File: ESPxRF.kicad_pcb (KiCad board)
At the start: 4 copper layers, 67.6 x 28.7 mm, 37 parts, among them J1 USB_C_Receptacle_USB2.0, J2 ANT, U1 NCP115ASN330T2G, U2 NRF24L01, U3 USBLC6-2SC6, U4 ESP32-S3, Y1 Crystal_GND24_Small

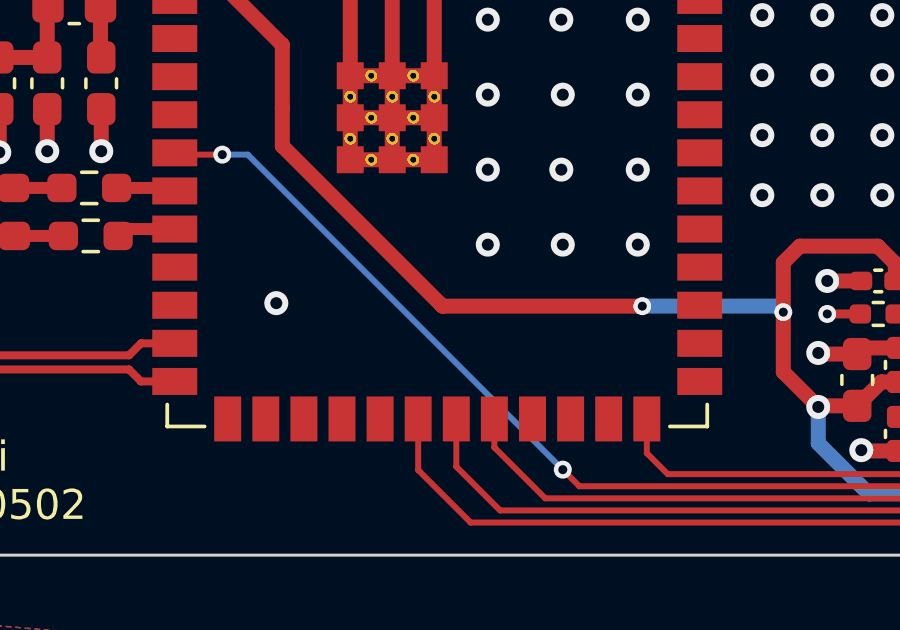
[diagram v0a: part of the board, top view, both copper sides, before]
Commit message: added jlc silkscreen tidied schematic
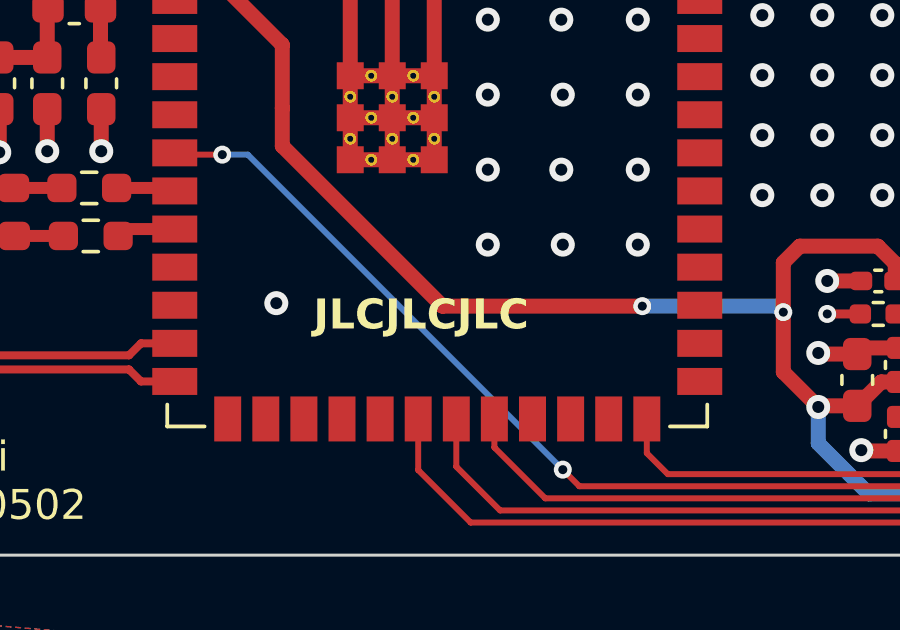
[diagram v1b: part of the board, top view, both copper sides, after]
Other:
- board text added: "JLCJLCJLC"
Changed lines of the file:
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@@
     (pad_to_mask_clearance 0)
     (pcbplotparams
-      (layerselection 0x00010fc_ffffffff)
+      (layerselection 0x00011fc_ffffffff)
       (plot_on_all_layers_selection 0x0000000_00000000)
       (disableapertmacros false)
@@
       (outputformat 1)
       (mirror false)
-      (drillshape 1)
+      (drillshape 0)
       (scaleselection 1)
-      (outputdirectory "")
+      (outputdirectory "Gerber/")
     )
   )
@@
     (fp_line (start 2 2) (end -2 2)
       (stroke (width 0.1) (type solid)) (layer "F.Fab"))
-    (pad "" smd roundrect (at -0.625 -0.625 90) (size 1.01 1.01) (layers "F.Paste") (roundrect_rratio 0.247525))
-    (pad "" smd roundrect (at -0.625 0.625 90) (size 1.01 1.01) (layers "F.Paste") (roundrect_rratio 0.247525))
-    (pad "" smd roundrect (at 0.625 -0.625 90) (size 1.01 1.01) (layers "F.Paste") (roundrect_rratio 0.247525))
-    (pad "" smd roundrect (at 0.625 0.625 90) (size 1.01 1.01) (layers "F.Paste") (roundrect_rratio 0.247525))
+    (pad "" smd roundrect (at -0.625 -0.625 90) (size 1.01 1.01) (layers "F.Paste") (roundrect_rratio 0.2475247525))
+    (pad "" smd roundrect (at -0.625 0.625 90) (size 1.01 1.01) (layers "F.Paste") (roundrect_rratio 0.2475247525))
+    (pad "" smd roundrect (at 0.625 -0.625 90) (size 1.01 1.01) (layers "F.Paste") (roundrect_rratio 0.2475247525))
+    (pad "" smd roundrect (at 0.625 0.625 90) (size 1.01 1.01) (layers "F.Paste") (roundrect_rratio 0.2475247525))
     (pad "1" smd roundrect (at -1.9375 -1 90) (size 0.825 0.25) (layers "F.Cu" "F.Paste" "F.Mask") (roundrect_rratio 0.25)
       (net 9 "CE") (pinfunction "CE") (pintype "input"))
@@
     (effects (font (size 1 1) (thickness 0.25) bold) (justify left bottom))
   )
+  (gr_text "JLCJLCJLC" (at 116.84 75.565) (layer "F.SilkS")
+    (effects (font (size 1 1) (thickness 0.25) bold) (justify left bottom))
+  )

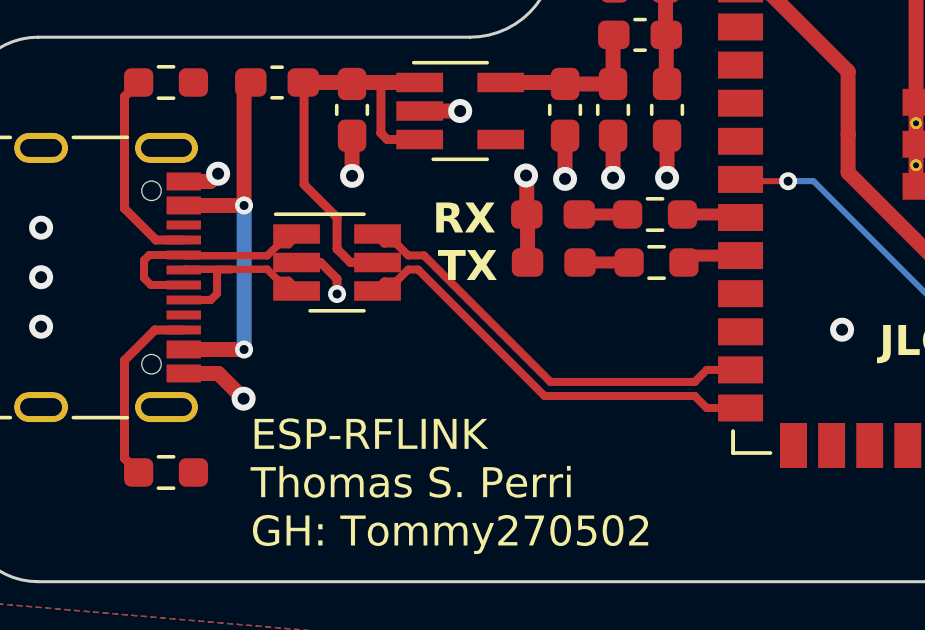
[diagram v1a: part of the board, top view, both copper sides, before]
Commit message: fixed short usb esd protection IC
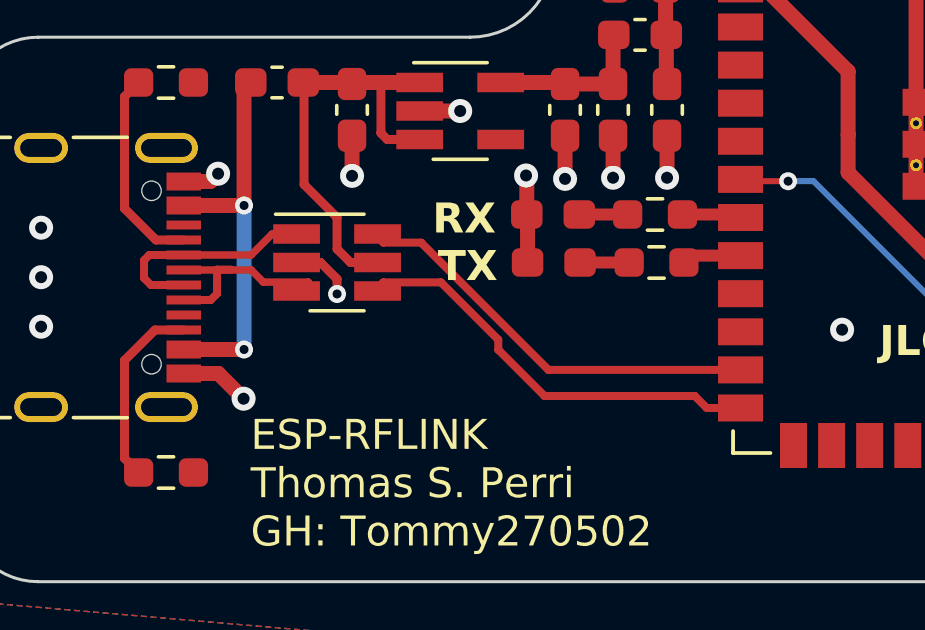
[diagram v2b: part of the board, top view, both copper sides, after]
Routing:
- net USBCON_D+: track 6.65 -> 7.22 mm
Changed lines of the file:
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@@
   (segment (start 137.0975 77.56) (end 136.265 78.3925) (width 0.2) (layer "F.Cu") (net 4))
   (segment (start 137.59 77.56) (end 137.0975 77.56) (width 0.2) (layer "F.Cu") (net 4))
-  (segment (start 93.655 72.61) (end 93.679999 72.585001) (width 0.25) (layer "F.Cu") (net 5))
   (segment (start 94.765163 73.398445) (end 94.765163 72.596803) (width 0.267208) (layer "F.Cu") (net 5))
   (segment (start 94.553608 73.61) (end 94.765163 73.398445) (width 0.267208) (layer "F.Cu") (net 5))
+  (segment (start 96.3068 73.0132) (end 97.8068 73.0132) (width 0.25) (layer "F.Cu") (net 5))
+  (segment (start 95.9036 72.61) (end 96.3068 73.0132) (width 0.25) (layer "F.Cu") (net 5))
   (segment (start 94.765163 72.596803) (end 95.25 72.596803) (width 0.267208) (layer "F.Cu") (net 5))
   (segment (start 93.655 73.61) (end 94.553608 73.61) (width 0.267208) (layer "F.Cu") (net 5))
-  (segment (start 97.155 72.955) (end 97.51 73.31) (width 0.25) (layer "F.Cu") (net 5))
-  (segment (start 96.43493 72.585001) (end 96.804929 72.955) (width 0.25) (layer "F.Cu") (net 5))
-  (segment (start 96.804929 72.955) (end 97.155 72.955) (width 0.25) (layer "F.Cu") (net 5))
-  (segment (start 93.679999 72.585001) (end 96.43493 72.585001) (width 0.25) (layer "F.Cu") (net 5))
+  (segment (start 93.655 72.61) (end 95.9036 72.61) (width 0.25) (layer "F.Cu") (net 5))
+  (segment (start 97.8068 73.0132) (end 97.51 73.31) (width 0.25) (layer "F.Cu") (net 5))
   (segment (start 139.51 75.105) (end 139.5275 75.1225) (width 0.2) (layer "F.Cu") (net 6))
   (segment (start 139.4825 69.29875) (end 139.4825 70.39875) (width 0.2) (layer "F.Cu") (net 6))
@@
   (via (at 95.665 70.46) (size 0.6) (drill 0.3) (layers "F.Cu" "B.Cu") (net 26))
   (segment (start 95.665 75.26) (end 95.665 70.46) (width 0.5) (layer "B.Cu") (net 26))
-  (segment (start 101.467574 72.595204) (end 105.682574 76.810204) (width 0.267208) (layer "F.Cu") (net 33))
-  (segment (start 100.338196 72.991804) (end 100.740316 72.991804) (width 0.267208) (layer "F.Cu") (net 33))
+  (segment (start 100.02 73.31) (end 100.308196 73.021804) (width 0.267208) (layer "F.Cu") (net 33))
+  (segment (start 105.682574 76.810204) (end 110.690203 76.810204) (width 0.267208) (layer "F.Cu") (net 33))
+  (segment (start 100.308196 73.021804) (end 102.22835 73.021804) (width 0.267208) (layer "F.Cu") (net 33))
+  (segment (start 104.14 74.933454) (end 104.14 75.26763) (width 0.267208) (layer "F.Cu") (net 33))
+  (segment (start 104.14 75.26763) (end 105.682574 76.810204) (width 0.267208) (layer "F.Cu") (net 33))
+  (segment (start 110.690203 76.810204) (end 111.089999 77.21) (width 0.267208) (layer "F.Cu") (net 33))
   (segment (start 111.089999 77.21) (end 112.215 77.21) (width 0.267208) (layer "F.Cu") (net 33))
-  (segment (start 100.740316 72.991804) (end 101.136916 72.595204) (width 0.267208) (layer "F.Cu") (net 33))
-  (segment (start 100.02 73.31) (end 100.338196 72.991804) (width 0.267208) (layer "F.Cu") (net 33))
-  (segment (start 110.690203 76.810204) (end 111.089999 77.21) (width 0.267208) (layer "F.Cu") (net 33))
-  (segment (start 101.136916 72.595204) (end 101.467574 72.595204) (width 0.267208) (layer "F.Cu") (net 33))
-  (segment (start 105.682574 76.810204) (end 110.690203 76.810204) (width 0.267208) (layer "F.Cu") (net 33))
-  (segment (start 101.662426 72.124796) (end 105.877426 76.339796) (width 0.267208) (layer "F.Cu") (net 34))
-  (segment (start 110.690203 76.339796) (end 111.089999 75.94) (width 0.267208) (layer "F.Cu") (net 34))
-  (segment (start 100.338196 71.728196) (end 100.740316 71.728196) (width 0.267208) (layer "F.Cu") (net 34))
-  (segment (start 111.089999 75.94) (end 112.215 75.94) (width 0.267208) (layer "F.Cu") (net 34))
-  (segment (start 105.877426 76.339796) (end 110.690203 76.339796) (width 0.267208) (layer "F.Cu") (net 34))
-  (segment (start 101.136916 72.124796) (end 101.662426 72.124796) (width 0.267208) (layer "F.Cu") (net 34))
-  (segment (start 100.02 71.41) (end 100.338196 71.728196) (width 0.267208) (layer "F.Cu") (net 34))
-  (segment (start 100.740316 71.728196) (end 101.136916 72.124796) (width 0.267208) (layer "F.Cu") (net 34))
-  (segment (start 96.43493 72.134999) (end 96.804929 71.765) (width 0.25) (layer "F.Cu") (net 56))
-  (segment (start 96.804929 71.765) (end 97.155 71.765) (width 0.25) (layer "F.Cu") (net 56))
+  (segment (start 102.22835 73.021804) (end 104.14 74.933454) (width 0.267208) (layer "F.Cu") (net 33))
+  (segment (start 100.308196 71.698196) (end 101.57 71.698196) (width 0.267208) (layer "F.Cu") (net 34))
+  (segment (start 100.02 71.41) (end 100.308196 71.698196) (width 0.267208) (layer "F.Cu") (net 34))
+  (segment (start 101.57 71.698196) (end 105.811804 75.94) (width 0.267208) (layer "F.Cu") (net 34))
+  (segment (start 105.811804 75.94) (end 112.215 75.94) (width 0.267208) (layer "F.Cu") (net 34))
+  (segment (start 95.9036 72.11) (end 96.6036 71.41) (width 0.25) (layer "F.Cu") (net 56))
   (segment (start 92.561168 73.11) (end 92.33155 72.880382) (width 0.267208) (layer "F.Cu") (net 56))
   (segment (start 92.33155 72.880382) (end 92.33155 72.287438) (width 0.267208) (layer "F.Cu") (net 56))
-  (segment (start 93.655 72.11) (end 93.679999 72.134999) (width 0.25) (layer "F.Cu") (net 56))
   (segment (start 93.655 73.11) (end 92.561168 73.11) (width 0.267208) (layer "F.Cu") (net 56))
   (segment (start 92.508988 72.11) (end 93.655 72.11) (width 0.267208) (layer "F.Cu") (net 56))
-  (segment (start 93.679999 72.134999) (end 96.43493 72.134999) (width 0.25) (layer "F.Cu") (net 56))
   (segment (start 92.33155 72.287438) (end 92.508988 72.11) (width 0.267208) (layer "F.Cu") (net 56))
-  (segment (start 97.155 71.765) (end 97.51 71.41) (width 0.25) (layer "F.Cu") (net 56))
+  (segment (start 96.6036 71.41) (end 97.51 71.41) (width 0.25) (layer "F.Cu") (net 56))
+  (segment (start 93.655 72.11) (end 95.9036 72.11) (width 0.25) (layer "F.Cu") (net 56))
   (segment (start 112.115 70.76) (end 112.215 70.86) (width 0.4) (layer "F.Cu") (net 57))
   (segment (start 110.2775 70.76) (end 112.115 70.76) (width 0.4) (layer "F.Cu") (net 57))
